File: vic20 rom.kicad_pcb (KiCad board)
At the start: 2 copper layers, 36 x 37.5 mm, 8 parts, among them J3 Basic Bank 2 S/W, J5 Kernel Bank 2 S/W, K2 En Kernel Bank 2 S/W

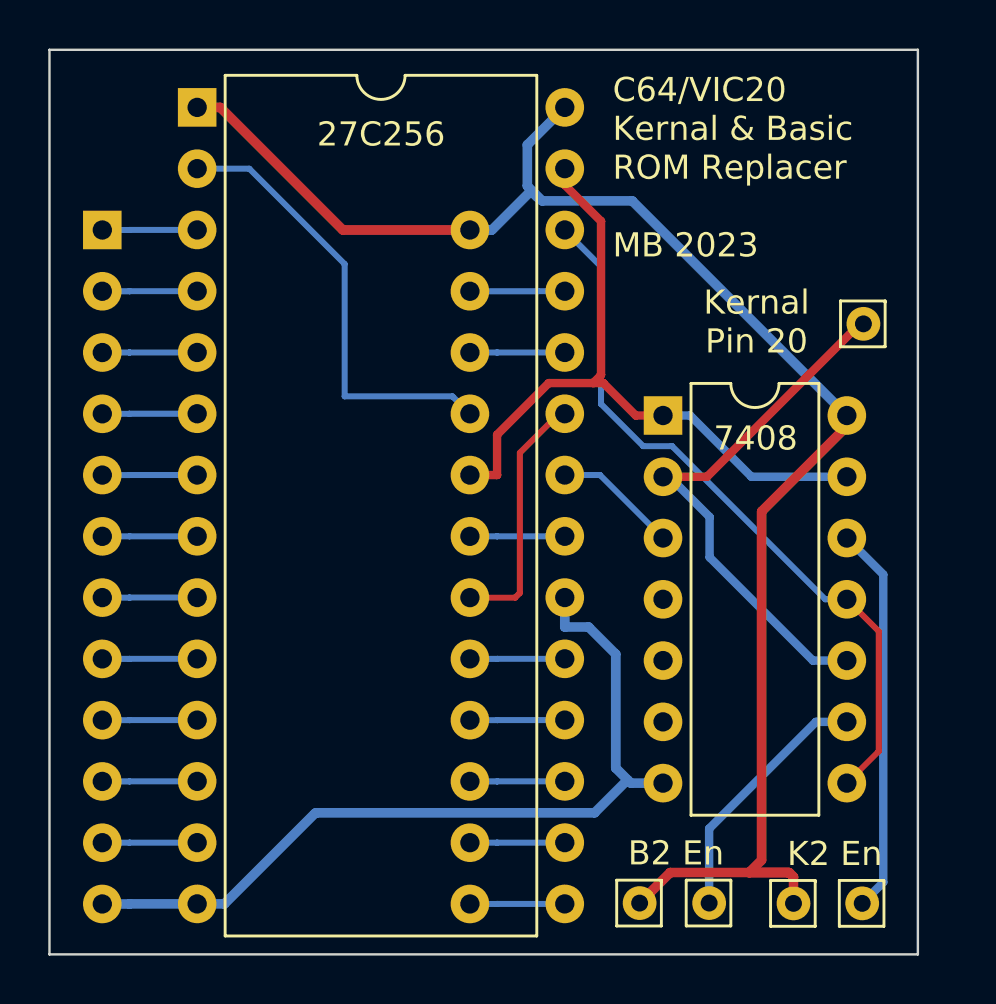
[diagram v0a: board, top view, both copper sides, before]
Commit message: Master: Added GND pin for switches
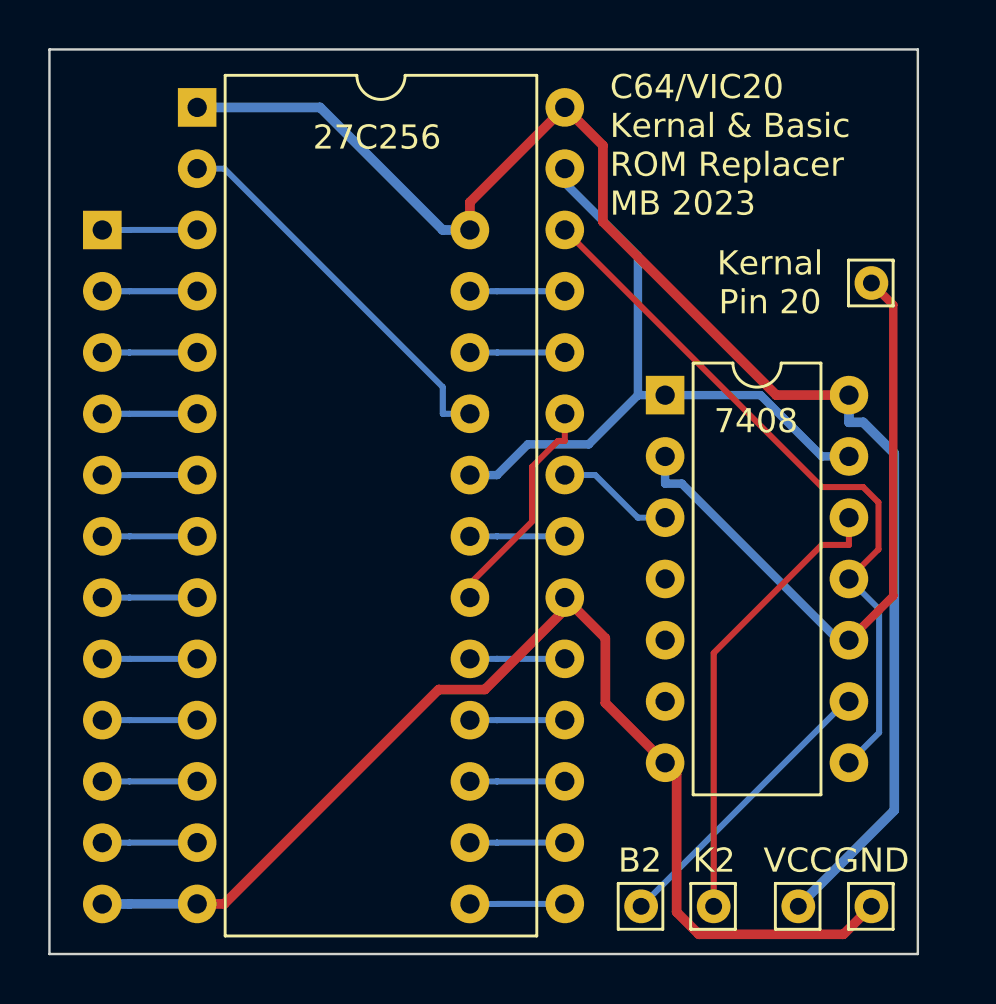
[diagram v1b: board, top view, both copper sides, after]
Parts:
- removed 7408: 74LS08, Package_DIP:DIP-14_W7.62mm
- removed K2 En: Kernel Bank 2 S/W, Connector_Pin:Pin_D0.7mm_L6.5mm_W1.8mm_FlatFork
- added GND1: GND, Connector_Pin:Pin_D0.7mm_L6.5mm_W1.8mm_FlatFork, F.Cu at (111.6, 79.0)
- added U2: 7408, Package_DIP:DIP-14_W7.62mm, F.Cu at (103.0, 57.8)
- J1: renamed from Kernal C/E
- S1: renamed from 8K ROM; value Basic Header -> 8K ROM
- VCC1: renamed from B2 En; value Basic Bank 2 S/W -> VCC
- moved VCC1 6.58 mm to (108.5, 79.0)
- moved K2 6.16 mm to (105.0, 79.0)
- moved B2 2.82 mm to (102.0, 79.0)
- moved J1 1.73 mm to (111.6, 53.2)
- renumbered J3 to B2, J5 to K2, 27C256 to U1
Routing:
- net Net-(GND1-Pin_1): track 34.6 -> 48.6 mm
- net Net-(S1-VCC): track 68.4 -> 62.7 mm
- net Net-(J1-Pin_1): track 22.4 -> 27.4 mm
- net Net-(K2-Pin_1): track 16.1 -> 19.1 mm
- net Net-(S1-A12): track 18.7 -> 16.2 mm
- net Net-(B2-Pin_1): track 10.6 -> 12.1 mm
- net Net-(S1-A11): track 10.5 -> 9.42 mm
- net Net-(S1-~{CE}): track 29.4 -> 28.8 mm

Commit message: Master: Added PCB images to readme file
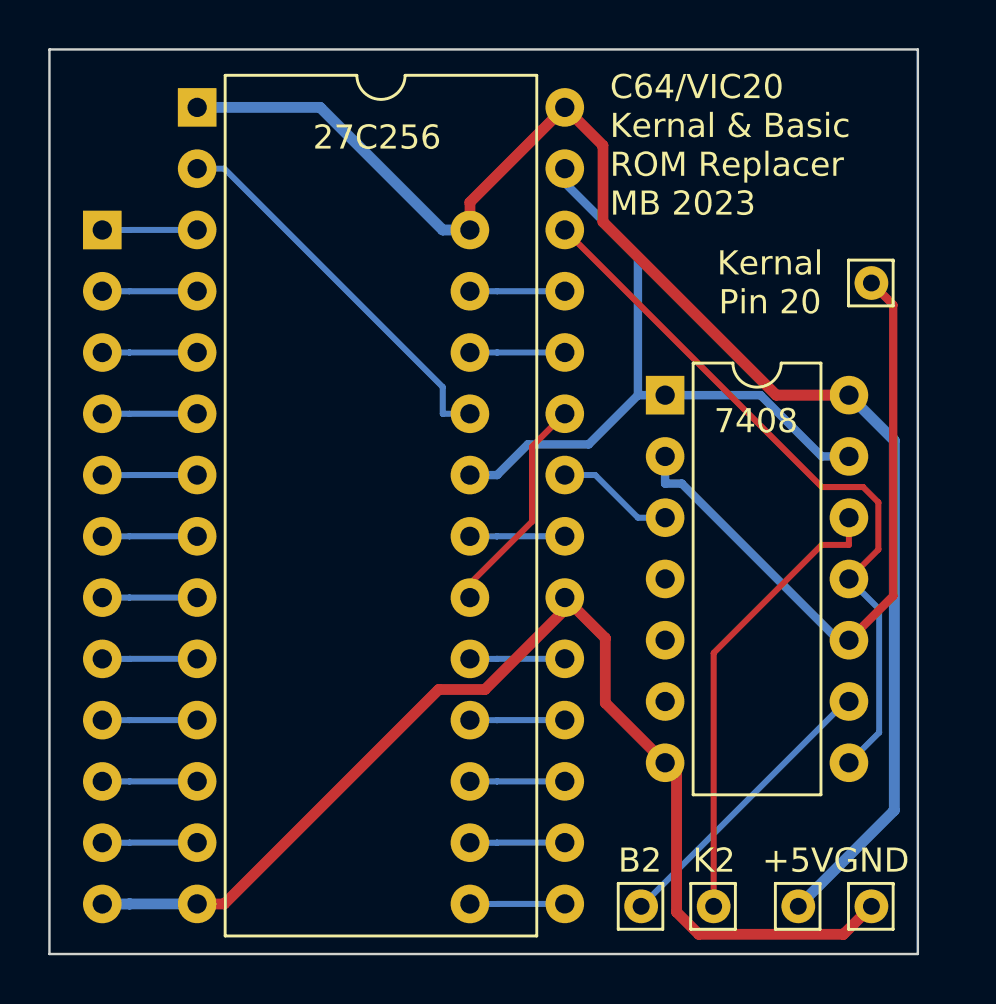
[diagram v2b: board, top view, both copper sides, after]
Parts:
- VCC1: value VCC -> +5V
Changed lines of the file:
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@@
     (pad_to_mask_clearance 0)
     (pcbplotparams
-      (layerselection 0x00010ec_ffffffff)
+      (layerselection 0x00010e0_ffffffff)
       (plot_on_all_layers_selection 0x0000000_00000000)
       (disableapertmacros false)
@@
         (effects (font (size 1 1) (thickness 0.15)))
     )
-    (fp_text value "VCC" (at -0.018429 -1.900674) (layer "F.SilkS")
+    (fp_text value "+5V" (at -0.018429 -1.900674) (layer "F.SilkS")
         (effects (font (size 1 1) (thickness 0.15)))
     )
@@
   (segment (start 103.0226 61.4835) (end 103.0226 60.3566) (width 0.35) (layer "B.Cu") (net 1))
   (segment (start 103.715112 61.4835) (end 103.0226 61.4835) (width 0.35) (layer "B.Cu") (net 1))
-  (segment (start 84.7493 78.9075) (end 93.6368 70.02) (width 0.4) (layer "F.Cu") (net 2))
-  (segment (start 95.550515 70.02) (end 98.8624 66.708115) (width 0.4) (layer "F.Cu") (net 2))
-  (segment (start 103.497976 79.245047) (end 104.420919 80.16799) (width 0.4) (layer "F.Cu") (net 2))
-  (segment (start 104.420919 80.16799) (end 110.41431 80.16799) (width 0.4) (layer "F.Cu") (net 2))
-  (segment (start 103.0226 73.0566) (end 103.497976 73.531976) (width 0.4) (layer "F.Cu") (net 2))
-  (segment (start 110.41431 80.16799) (end 111.5743 79.008) (width 0.4) (layer "F.Cu") (net 2))
-  (segment (start 93.6368 70.02) (end 95.550515 70.02) (width 0.4) (layer "F.Cu") (net 2))
-  (segment (start 98.8624 66.2075) (end 100.543343 67.888443) (width 0.4) (layer "F.Cu") (net 2))
-  (segment (start 83.6224 78.9075) (end 84.7493 78.9075) (width 0.4) (layer "F.Cu") (net 2))
-  (segment (start 100.543343 67.888443) (end 100.543343 70.577343) (width 0.4) (layer "F.Cu") (net 2))
-  (segment (start 103.497976 73.531976) (end 103.497976 79.245047) (width 0.4) (layer "F.Cu") (net 2))
-  (segment (start 98.8624 66.708115) (end 98.8624 66.2075) (width 0.4) (layer "F.Cu") (net 2))
-  (segment (start 100.543343 70.577343) (end 103.0226 73.0566) (width 0.4) (layer "F.Cu") (net 2))
-  (segment (start 80.8194 78.9075) (end 80.8169 78.91) (width 0.4) (layer "B.Cu") (net 2))
-  (segment (start 83.6224 78.9075) (end 80.8194 78.9075) (width 0.4) (layer "B.Cu") (net 2))
-  (segment (start 79.69 78.91) (end 80.8169 78.91) (width 0.4) (layer "B.Cu") (net 2))
+  (segment (start 84.7493 78.9075) (end 93.6368 70.02) (width 0.45) (layer "F.Cu") (net 2))
+  (segment (start 95.550515 70.02) (end 98.8624 66.708115) (width 0.45) (layer "F.Cu") (net 2))
+  (segment (start 103.497976 79.245047) (end 104.420919 80.16799) (width 0.45) (layer "F.Cu") (net 2))
+  (segment (start 104.420919 80.16799) (end 110.41431 80.16799) (width 0.45) (layer "F.Cu") (net 2))
+  (segment (start 103.0226 73.0566) (end 103.497976 73.531976) (width 0.45) (layer "F.Cu") (net 2))
+  (segment (start 110.41431 80.16799) (end 111.5743 79.008) (width 0.45) (layer "F.Cu") (net 2))
+  (segment (start 93.6368 70.02) (end 95.550515 70.02) (width 0.45) (layer "F.Cu") (net 2))
+  (segment (start 98.8624 66.2075) (end 100.543343 67.888443) (width 0.45) (layer "F.Cu") (net 2))
+  (segment (start 83.6224 78.9075) (end 84.7493 78.9075) (width 0.45) (layer "F.Cu") (net 2))
+  (segment (start 100.543343 67.888443) (end 100.543343 70.577343) (width 0.45) (layer "F.Cu") (net 2))
+  (segment (start 103.497976 73.531976) (end 103.497976 79.245047) (width 0.45) (layer "F.Cu") (net 2))
+  (segment (start 98.8624 66.708115) (end 98.8624 66.2075) (width 0.45) (layer "F.Cu") (net 2))
+  (segment (start 100.543343 70.577343) (end 103.0226 73.0566) (width 0.45) (layer "F.Cu") (net 2))
+  (segment (start 80.8194 78.9075) (end 80.8169 78.91) (width 0.45) (layer "B.Cu") (net 2))
+  (segment (start 83.6224 78.9075) (end 80.8194 78.9075) (width 0.45) (layer "B.Cu") (net 2))
+  (segment (start 79.69 78.91) (end 80.8169 78.91) (width 0.45) (layer "B.Cu") (net 2))
   (segment (start 110.6426 70.5166) (end 110.5189 70.5166) (width 0.25) (layer "B.Cu") (net 3))
   (segment (start 110.5189 70.5166) (end 102.0275 79.008) (width 0.25) (layer "B.Cu") (net 3))
@@
   (segment (start 96.0594 68.7475) (end 96.0569 68.75) (width 0.25) (layer "B.Cu") (net 20))
   (segment (start 98.8624 68.7475) (end 96.0594 68.7475) (width 0.25) (layer "B.Cu") (net 20))
-  (segment (start 98.8624 59.7144) (end 98.5806 59.7144) (width 0.25) (layer "F.Cu") (net 21))
+  (segment (start 98.8624 58.5875) (end 97.504201 59.945699) (width 0.25) (layer "F.Cu") (net 21))
   (segment (start 97.504201 63.059433) (end 94.93 65.633634) (width 0.25) (layer "F.Cu") (net 21))
   (segment (start 94.93 65.633634) (end 94.93 66.21) (width 0.25) (layer "F.Cu") (net 21))
-  (segment (start 98.8624 58.5875) (end 98.8624 59.7144) (width 0.25) (layer "F.Cu") (net 21))
-  (segment (start 98.5806 59.7144) (end 97.504201 60.790799) (width 0.25) (layer "F.Cu") (net 21))
-  (segment (start 97.504201 60.790799) (end 97.504201 63.059433) (width 0.25) (layer "F.Cu") (net 21))
+  (segment (start 97.504201 59.945699) (end 97.504201 63.059433) (width 0.25) (layer "F.Cu") (net 21))
   (segment (start 98.8624 63.6675) (end 96.0594 63.6675) (width 0.25) (layer "B.Cu") (net 22))
   (segment (start 94.93 63.67) (end 96.0569 63.67) (width 0.25) (layer "B.Cu") (net 22))
@@
   (segment (start 111.89536 71.80384) (end 110.6426 73.0566) (width 0.25) (layer "B.Cu") (net 28))
   (segment (start 111.89536 66.68936) (end 111.89536 71.80384) (width 0.25) (layer "B.Cu") (net 28))
-  (segment (start 98.8624 45.8875) (end 94.93 49.8199) (width 0.4) (layer "F.Cu") (net 29))
-  (segment (start 100.443686 47.468786) (end 100.443686 50.631719) (width 0.4) (layer "F.Cu") (net 29))
-  (segment (start 107.628567 57.8166) (end 110.6426 57.8166) (width 0.4) (layer "F.Cu") (net 29))
-  (segment (start 94.93 49.8199) (end 94.93 50.97) (width 0.4) (layer "F.Cu") (net 29))
-  (segment (start 100.443686 50.631719) (end 107.628567 57.8166) (width 0.4) (layer "F.Cu") (net 29))
-  (segment (start 98.8624 45.8875) (end 100.443686 47.468786) (width 0.4) (layer "F.Cu") (net 29))
-  (segment (start 83.6224 45.8875) (end 88.7206 45.8875) (width 0.4) (layer "B.Cu") (net 29))
-  (segment (start 112.522036 60.228618) (end 112.522036 75.028864) (width 0.4) (layer "B.Cu") (net 29))
-  (segment (start 94.93 50.97) (end 93.8031 50.97) (width 0.4) (layer "B.Cu") (net 29))
-  (segment (start 110.6426 57.8166) (end 110.6426 58.9435) (width 0.4) (layer "B.Cu") (net 29))
-  (segment (start 110.6426 58.9435) (end 111.236918 58.9435) (width 0.4) (layer "B.Cu") (net 29))
-  (segment (start 112.522036 75.028864) (end 108.5429 79.008) (width 0.4) (layer "B.Cu") (net 29))
-  (segment (start 111.236918 58.9435) (end 112.522036 60.228618) (width 0.4) (layer "B.Cu") (net 29))
-  (segment (start 88.7206 45.8875) (end 93.8031 50.97) (width 0.4) (layer "B.Cu") (net 29))
+  (segment (start 98.8624 45.8875) (end 94.93 49.8199) (width 0.45) (layer "F.Cu") (net 29))
+  (segment (start 100.443686 47.468786) (end 100.443686 50.631719) (width 0.45) (layer "F.Cu") (net 29))
+  (segment (start 107.628567 57.8166) (end 110.6426 57.8166) (width 0.45) (layer "F.Cu") (net 29))
+  (segment (start 94.93 49.8199) (end 94.93 50.97) (width 0.45) (layer "F.Cu") (net 29))
+  (segment (start 100.443686 50.631719) (end 107.628567 57.8166) (width 0.45) (layer "F.Cu") (net 29))
+  (segment (start 98.8624 45.8875) (end 100.443686 47.468786) (width 0.45) (layer "F.Cu") (net 29))
+  (segment (start 83.6224 45.8875) (end 88.7206 45.8875) (width 0.45) (layer "B.Cu") (net 29))
+  (segment (start 94.93 50.97) (end 93.8031 50.97) (width 0.45) (layer "B.Cu") (net 29))
+  (segment (start 110.6426 57.8166) (end 112.522036 59.696036) (width 0.45) (layer "B.Cu") (net 29))
+  (segment (start 112.522036 75.028864) (end 108.5429 79.008) (width 0.45) (layer "B.Cu") (net 29))
+  (segment (start 112.522036 59.696036) (end 112.522036 75.028864) (width 0.45) (layer "B.Cu") (net 29))
+  (segment (start 88.7206 45.8875) (end 93.8031 50.97) (width 0.45) (layer "B.Cu") (net 29))
 )
